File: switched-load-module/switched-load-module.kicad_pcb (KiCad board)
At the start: 2 copper layers, 60 x 55 mm, 33 parts, among them J1 Conn_01x03, J2 Screw_Terminal_01x04, J3 Conn_01x03, J4 Screw_Terminal_01x05, Q1 BCW66H, Q2 Q_NMOS_GDS, U1 PC817, U2 L78L05_SOT89, U3 HFBR-2521Z, U4 DGD0211C

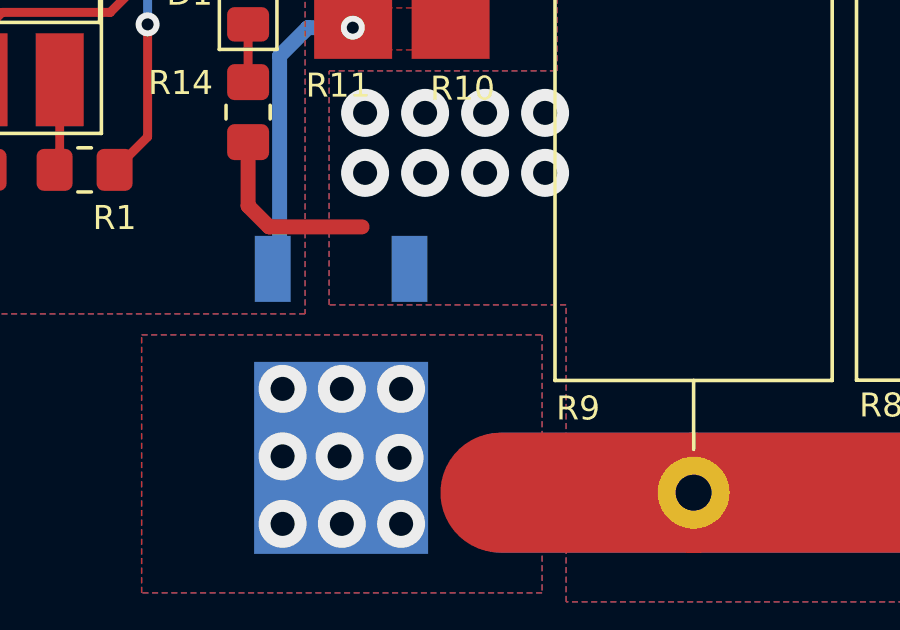
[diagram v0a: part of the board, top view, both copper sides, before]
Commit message: Added diode for switched load module
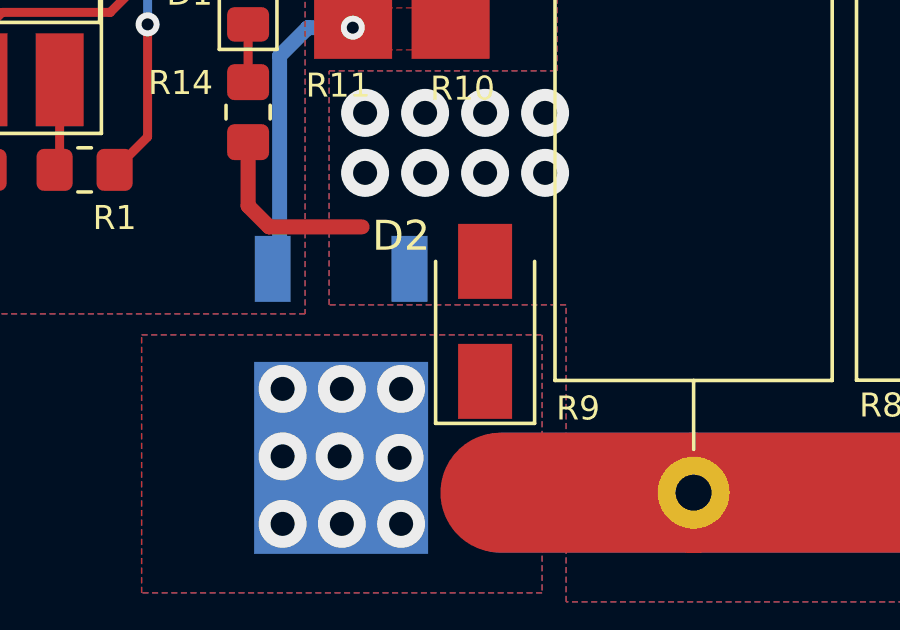
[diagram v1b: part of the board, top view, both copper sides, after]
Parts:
- added D2: D, Diode_SMD:D_SMA, F.Cu at (62.1, 88.9)
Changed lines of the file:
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@@
+    )
+  )
+  (footprint "Diode_SMD:D_SMA" (layer "F.Cu")
+    (at 62.15 88.9 90)
+    (descr "Diode SMA (DO-214AC)")
+    (tags "Diode SMA (DO-214AC)")
+    (property "Sheetfile" "switched-load-module.kicad_sch")
+    (property "Sheetname" "")
+    (attr smd)
+    (fp_text reference "D2" (at 2.85 -2.8 180) (layer "F.SilkS")
+      (effects (font (size 1 1) (thickness 0.15)))
+    )
+    (fp_text value "D" (at 0 2.6 90) (layer "F.Fab")
+      (effects (font (size 1 1) (thickness 0.15)))
+    )
+    (fp_text user "${REFERENCE}" (at 0 -2.5 90) (layer "F.Fab")
+      (effects (font (size 1 1) (thickness 0.15)))
+    )
+    (fp_line (start -3.4 -1.65) (end 2 -1.65) (layer "F.SilkS") (width 0.12))
+    (fp_line (start -3.4 1.65) (end 2 1.65) (layer "F.SilkS") (width 0.12))
+    (fp_line (start -3.4 -1.65) (end -3.4 1.65) (layer "F.SilkS") (width 0.12))
+    (fp_line (start 3.5 1.75) (end -3.5 1.75) (layer "F.CrtYd") (width 0.05))
+    (fp_line (start -3.5 -1.75) (end 3.5 -1.75) (layer "F.CrtYd") (width 0.05))
+    (fp_line (start 3.5 -1.75) (end 3.5 1.75) (layer "F.CrtYd") (width 0.05))
+    (fp_line (start -3.5 1.75) (end -3.5 -1.75) (layer "F.CrtYd") (width 0.05))
+    (fp_line (start 2.3 1.5) (end -2.3 1.5) (layer "F.Fab") (width 0.1))
+    (fp_line (start 0.50118 0.75032) (end 0.50118 -0.79908) (layer "F.Fab") (width 0.1))
+    (fp_line (start -0.64944 -0.79908) (end -0.64944 0.80112) (layer "F.Fab") (width 0.1))
+    (fp_line (start -2.3 1.5) (end -2.3 -1.5) (layer "F.Fab") (width 0.1))
+    (fp_line (start -0.64944 0.00102) (end 0.50118 0.75032) (layer "F.Fab") (width 0.1))
+    (fp_line (start 0.50118 0.00102) (end 1.4994 0.00102) (layer "F.Fab") (width 0.1))
+    (fp_line (start 2.3 -1.5) (end 2.3 1.5) (layer "F.Fab") (width 0.1))
+    (fp_line (start -0.64944 0.00102) (end 0.50118 -0.79908) (layer "F.Fab") (width 0.1))
+    (fp_line (start -0.64944 0.00102) (end -1.55114 0.00102) (layer "F.Fab") (width 0.1))
+    (fp_line (start 2.3 -1.5) (end -2.3 -1.5) (layer "F.Fab") (width 0.1))
+    (pad "1" smd rect (at -2 0 90) (size 2.5 1.8) (layers "F.Cu" "F.Paste" "F.Mask")
+      (net 10 "/LOAD_N") (pinfunction "K") (pintype "passive"))
+    (pad "2" smd rect (at 2 0 90) (size 2.5 1.8) (layers "F.Cu" "F.Paste" "F.Mask")
+      (net 1 "GNDA") (pinfunction "A") (pintype "passive"))
+    (model "${KICAD6_3DMODEL_DIR}/Diode_SMD.3dshapes/D_SMA.wrl"
+      (offset (xyz 0 0 0))
+      (scale (xyz 1 1 1))
+      (rotate (xyz 0 0 0))
     )
   )

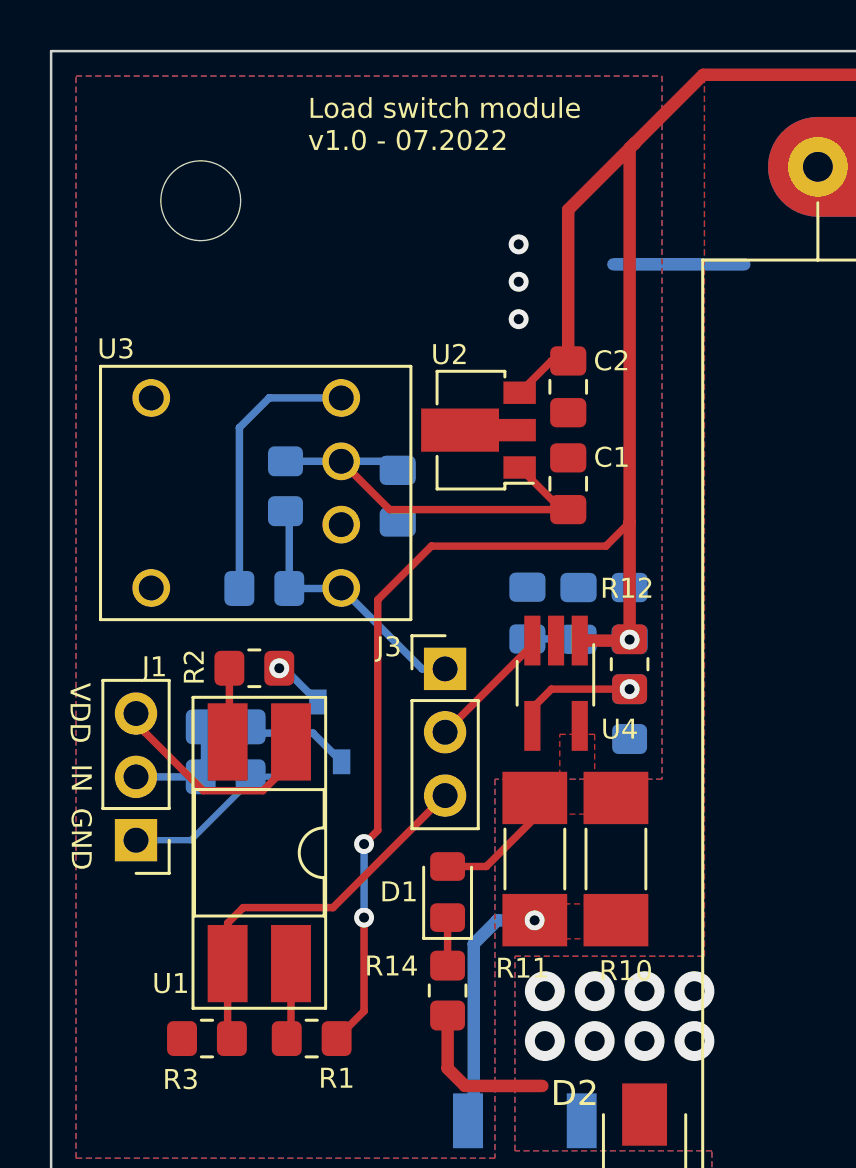
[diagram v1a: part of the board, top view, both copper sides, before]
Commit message: Added LEDs to switched load module
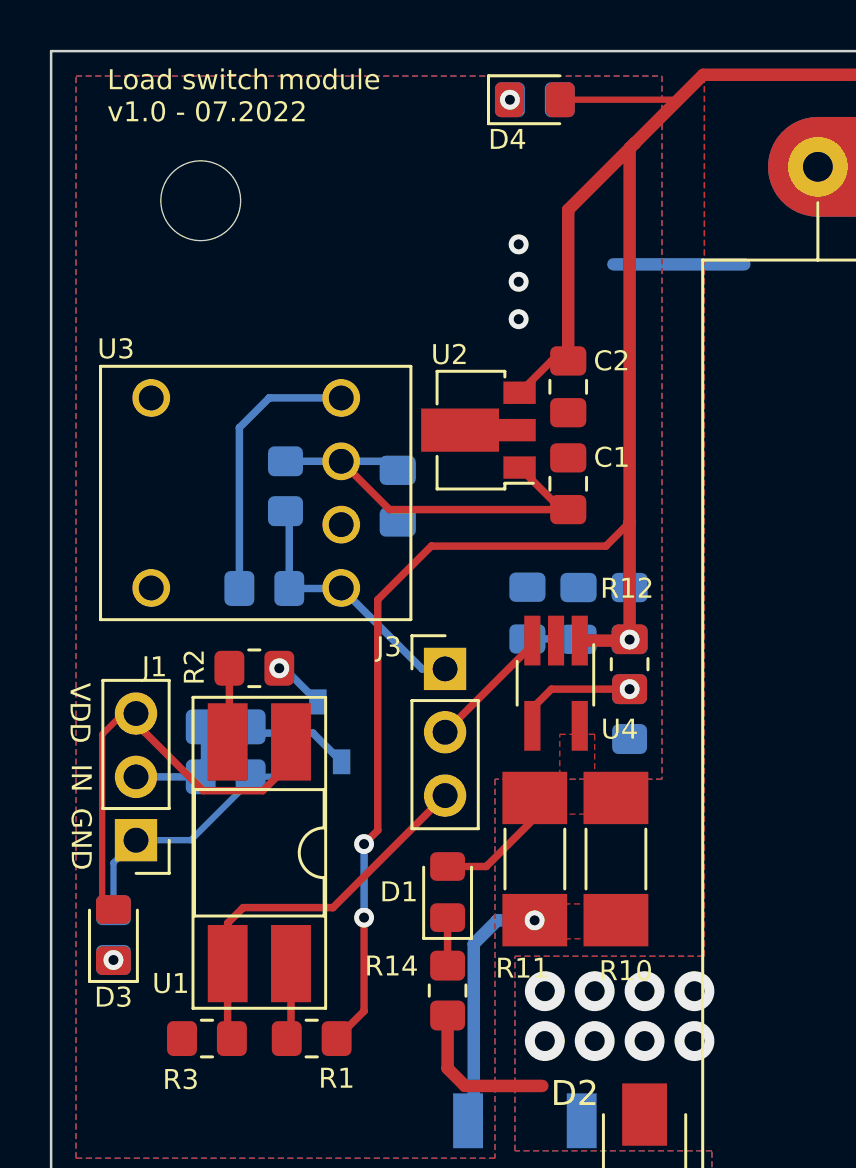
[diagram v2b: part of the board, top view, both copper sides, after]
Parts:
- added D3: LED, LED_SMD:LED_0805_2012Metric_Pad1.15x1.40mm_HandSolder, F.Cu at (40.9, 79.7)
- added D4: LED, LED_SMD:LED_0805_2012Metric_Pad1.15x1.40mm_HandSolder, F.Cu at (57.8, 46.2)
- added R15: 2k, Resistor_SMD:R_0805_2012Metric_Pad1.20x1.40mm_HandSolder, B.Cu at (40.9, 79.7)
- added R16: 2k, Resistor_SMD:R_0805_2012Metric_Pad1.20x1.40mm_HandSolder, B.Cu at (57.8, 46.2)
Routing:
- net VDD: track 8.88 -> 17.8 mm
- net VDDA: track 102.4 -> 108.6 mm
- net GNDD: track 7.30 -> 10.5 mm
- net Net-(D4-Pad1): vias 0 -> 1
- net Net-(D3-Pad1): vias 0 -> 1

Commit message: Added/fixed mounting holes
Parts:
- removed ?: , 
- added REF**: MountingHole_3.2mm_M3, MountingHole:MountingHole_3.2mm_M3, F.Cu at (44.4, 93.2)
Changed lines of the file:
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@@
     )
+  )
+  (footprint "MountingHole:MountingHole_3.2mm_M3" (layer "F.Cu")
+    (at 44.35 93.25)
+    (descr "Mounting Hole 3.2mm, no annular, M3")
+    (tags "mounting hole 3.2mm no annular m3")
+    (attr exclude_from_pos_files exclude_from_bom)
+    (fp_text reference "REF**" (at 0 -4.2) (layer "F.SilkS") hide
+      (effects (font (size 1 1) (thickness 0.15)))
+    )
+    (fp_text value "MountingHole_3.2mm_M3" (at 0 4.2) (layer "F.Fab") hide
+      (effects (font (size 1 1) (thickness 0.15)))
+    )
+    (fp_text user "${REFERENCE}" (at 0 0) (layer "F.Fab")
+      (effects (font (size 1 1) (thickness 0.15)))
+    )
+    (fp_circle (center 0 0) (end 3.2 0) (layer "Cmts.User") (width 0.15) (fill none))
+    (fp_circle (center 0 0) (end 3.45 0) (layer "F.CrtYd") (width 0.05) (fill none))
+    (pad "" np_thru_hole circle (at 0 0) (size 3.2 3.2) (drill 3.2) (layers *.Cu *.Mask))
   )
   (footprint "Resistor_SMD:R_MELF_MMB-0207" (layer "F.Cu")
@@
       (effects (font (size 1 1) (thickness 0.15)))
     )
-    (fp_text value "MountingHole_3.2mm_M3" (at 0 4.2) (layer "F.Fab")
+    (fp_text value "MountingHole_3.2mm_M3" (at 0 4.2) (layer "F.Fab") hide
       (effects (font (size 1 1) (thickness 0.15)))
     )
@@
     )
   )
-  (footprint "" (layer "F.Cu")
-    (at 44.35 93.25)
-    (fp_text reference "" (at 0 0) (layer "F.SilkS")
-      (effects (font (size 1.27 1.27) (thickness 0.15)))
-    )
-    (fp_text value "" (at 0 0) (layer "F.SilkS")
-      (effects (font (size 1.27 1.27) (thickness 0.15)))
-    )
-    (pad "" np_thru_hole circle (at 0 0) (size 3.2 3.2) (drill 3.2) (layers *.Cu *.Mask))
-  )
   (footprint "Package_TO_SOT_SMD:SOT-89-3" (layer "F.Cu")

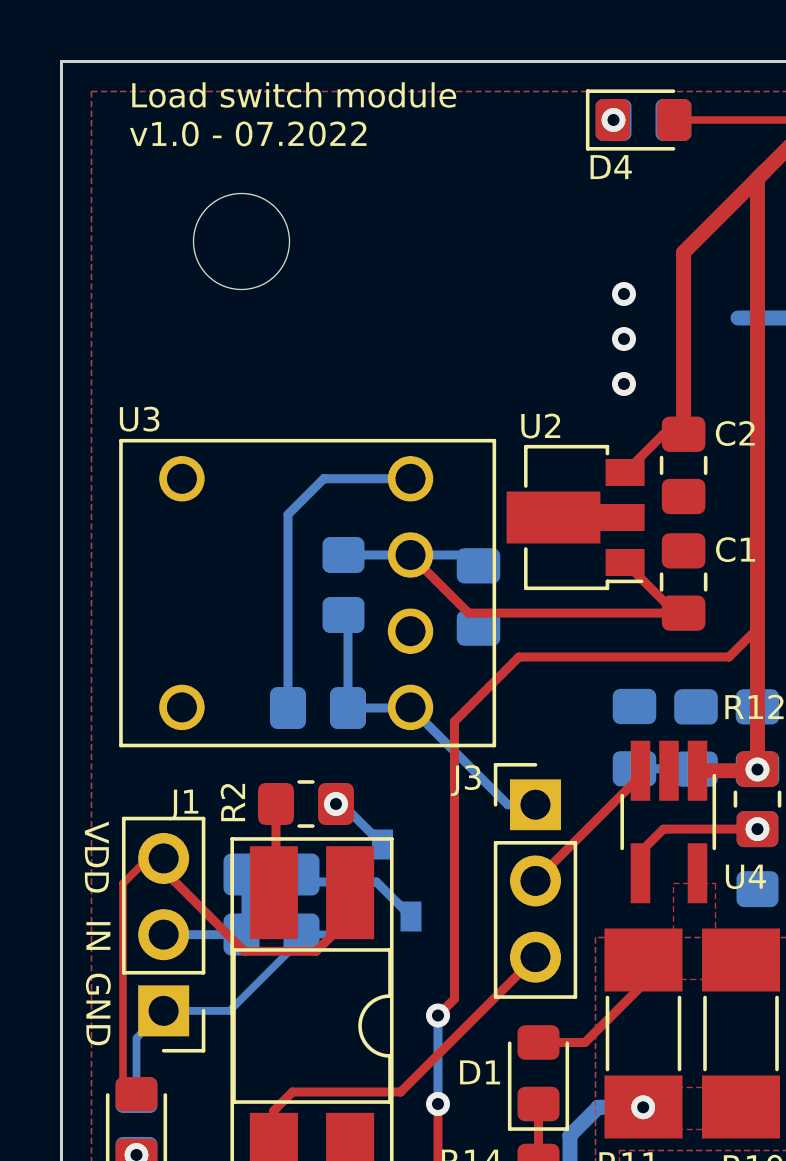
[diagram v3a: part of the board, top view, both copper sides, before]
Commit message: Updated boards with dates, silk, mounting holes
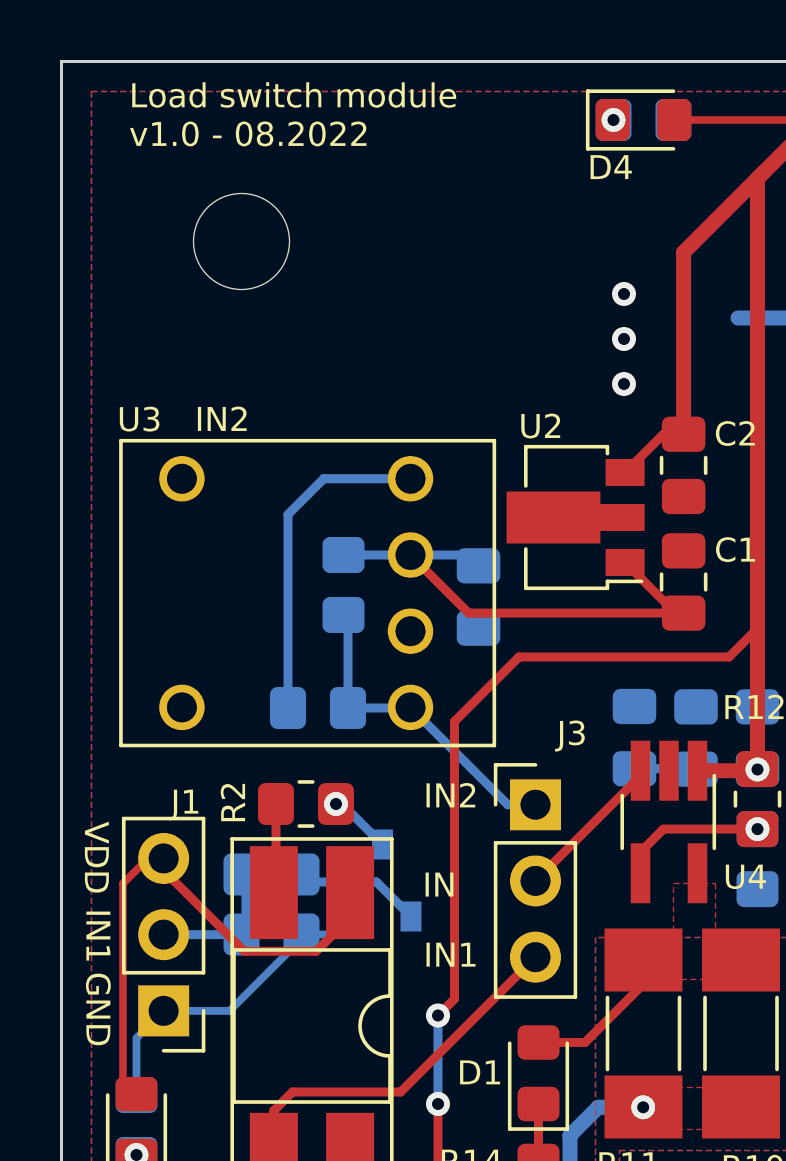
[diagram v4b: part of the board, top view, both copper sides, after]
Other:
- board text added: "IN1"
- board text added: "IN2"
- board text added: "Load switch module v1.0 - 08.2022"
- board text removed: "Load switch module v1.0 - 07.2022"
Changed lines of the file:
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@@
   (net 19 "Net-(R6-Pad2)")
   (net 20 "Net-(R12-Pad1)")
-  (net 21 "unconnected-(U3-Pad5)")
-  (net 22 "unconnected-(U3-Pad8)")
+  (net 21 "unconnected-(U3-Pad8)")
+  (net 22 "unconnected-(U3-Pad5)")
   (net 23 "Net-(D3-Pad1)")
   (net 24 "Net-(D4-Pad1)")
@@
       (effects (font (size 1 1) (thickness 0.15)))
     )
+    (fp_line (start -5.08 -6.35) (end -5.08 6.096) (layer "F.SilkS") (width 0.12))
+    (fp_line (start 5.08 6.096) (end 5.08 -6.35) (layer "F.SilkS") (width 0.12))
+    (fp_line (start -5.08 6.096) (end 5.08 6.096) (layer "F.SilkS") (width 0.12))
     (fp_line (start 5.08 -6.35) (end -5.08 -6.35) (layer "F.SilkS") (width 0.12))
-    (fp_line (start 5.08 6.096) (end 5.08 -6.35) (layer "F.SilkS") (width 0.12))
-    (fp_line (start -5.08 -6.35) (end -5.08 6.096) (layer "F.SilkS") (width 0.12))
-    (fp_line (start -5.08 6.096) (end 5.08 6.096) (layer "F.SilkS") (width 0.12))
     (pad "1" thru_hole circle (at -3.81 3.302 90) (size 1.515 1.515) (drill 1) (layers *.Cu *.Mask)
       (net 11 "/IN_A2") (pinfunction "Vo") (pintype "output"))
@@
       (net 19 "Net-(R6-Pad2)") (pinfunction "RL") (pintype "input"))
     (pad "5" thru_hole circle (at 3.81 -4.318 90) (size 1.515 1.515) (drill 1) (layers *.Cu *.Mask)
-      (net 21 "unconnected-(U3-Pad5)") (pinfunction "NC") (pintype "no_connect"))
+      (net 22 "unconnected-(U3-Pad5)") (pinfunction "NC") (pintype "no_connect"))
     (pad "8" thru_hole circle (at -3.81 -4.318 90) (size 1.515 1.515) (drill 1) (layers *.Cu *.Mask)
-      (net 22 "unconnected-(U3-Pad8)") (pinfunction "NC") (pintype "no_connect"))
+      (net 21 "unconnected-(U3-Pad8)") (pinfunction "NC") (pintype "no_connect"))
+    (model "${KICAD_USER_LIBRARY}/3d/CL_Fiber_Optic/HFBR2521.STEP"
+      (offset (xyz 0 3.25 0))
+      (scale (xyz 1 1 1))
+      (rotate (xyz 0 0 -90))
+    )
   )
   (footprint "Capacitor_SMD:C_0805_2012Metric_Pad1.18x1.45mm_HandSolder" (layer "F.Cu")
@@
     (property "Sheetname" "")
     (attr through_hole)
-    (fp_text reference "J3" (at -2.25 -0.875) (layer "F.SilkS")
+    (fp_text reference "J3" (at 1.2194 -2.3642) (layer "F.SilkS")
       (effects (font (size 0.8 0.8) (thickness 0.15)))
     )
@@
     (effects (font (size 0.8 0.8) (thickness 0.2)))
   )
-  (gr_text "Load switch module\nv1.0 - 07.2022" (at 40.6 46.05) (layer "F.SilkS")
+  (gr_text "Load switch module\nv1.0 - 08.2022" (at 40.6 46.05) (layer "F.SilkS")
     (effects (font (size 0.8 0.8) (thickness 0.2)) (justify left))
   )
@@
     (effects (font (size 0.8 0.8) (thickness 0.2)))
   )
+  (gr_text "IN2" (at 43.7108 56.196) (layer "F.SilkS")
+    (effects (font (size 0.8 0.8) (thickness 0.2)))
+  )
   (gr_text "VDD" (at 39.5 70.8 270) (layer "F.SilkS")
     (effects (font (size 0.8 0.8) (thickness 0.2)))
@@
     (effects (font (size 0.8 0.8) (thickness 0.2)))
   )
-  (gr_text "IN" (at 39.55 73.4 270) (layer "F.SilkS")
+  (gr_text "IN1" (at 39.55 73.4 270) (layer "F.SilkS")
     (effects (font (size 0.8 0.8) (thickness 0.2)))
   )
@@
     (effects (font (size 0.8 0.8) (thickness 0.2)))
   )
+  (gr_text "IN1" (at 51.3308 74.0522) (layer "F.SilkS")
+    (effects (font (size 0.8 0.8) (thickness 0.2)))
+  )
+  (gr_text "IN" (at 50.949848 71.7154) (layer "F.SilkS")
+    (effects (font (size 0.8 0.8) (thickness 0.2)))
+  )
   (gr_text "VBUS" (at 96.525 54.817856 90) (layer "F.SilkS")
     (effects (font (size 0.8 0.8) (thickness 0.2)))
@@
     (effects (font (size 0.8 0.8) (thickness 0.2)))
   )
+  (gr_text "IN2" (at 51.3308 68.7436) (layer "F.SilkS")
+    (effects (font (size 0.8 0.8) (thickness 0.2)))
+  )
